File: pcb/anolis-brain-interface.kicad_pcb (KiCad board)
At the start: 2 copper layers, 2 parts, among them U1 RHD2216, U2 Setebos-I

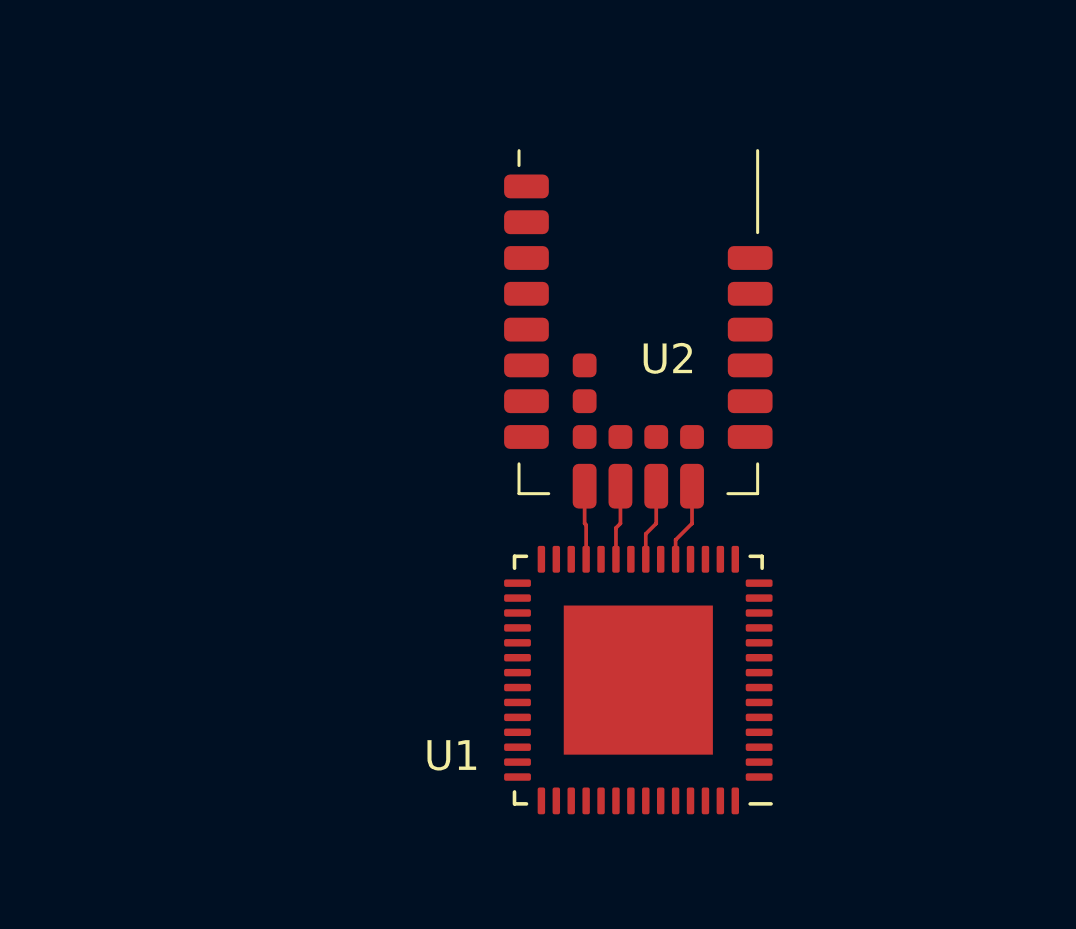
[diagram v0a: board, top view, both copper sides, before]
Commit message: Added uSD socket.
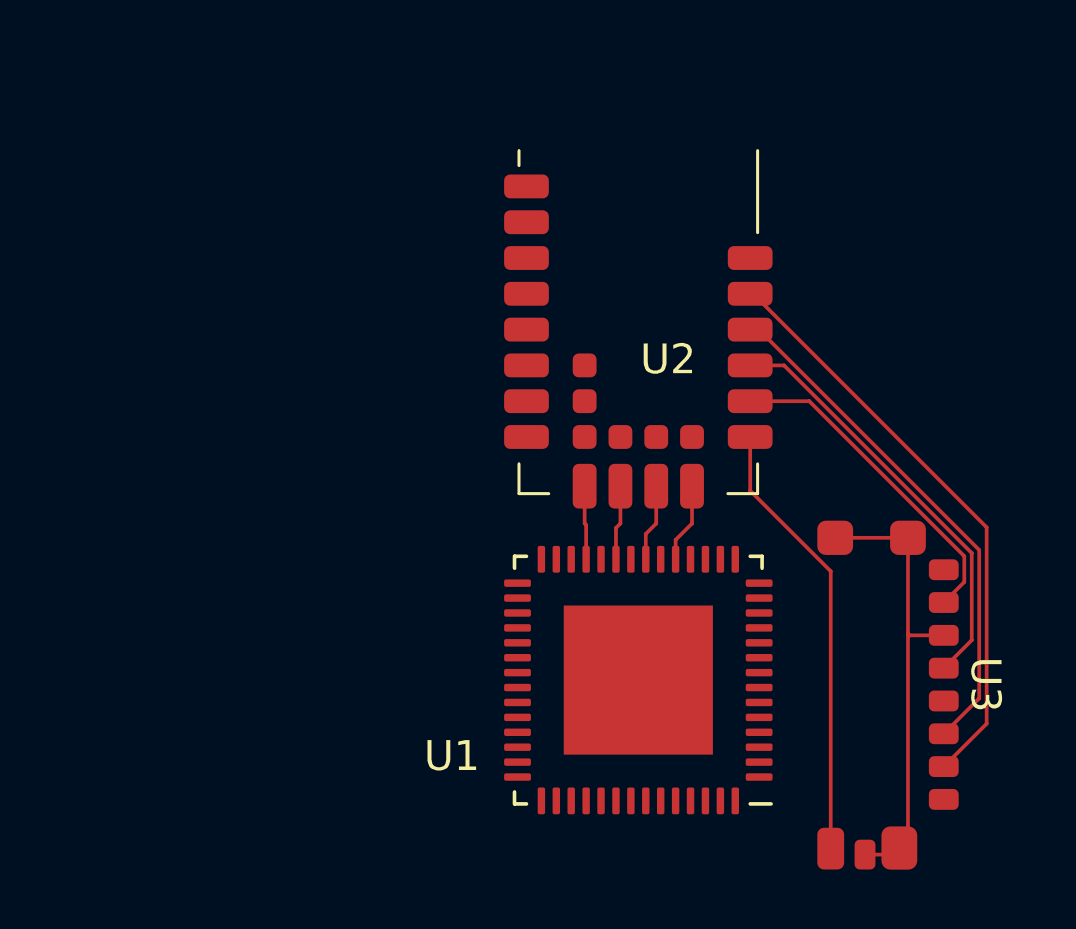
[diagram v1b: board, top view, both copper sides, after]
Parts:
- added U3: 47571-0001, sd:475710001, F.Cu at (155.6, 100.9)
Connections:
- U2 pad 13: unconnected-(U2-P1.08-Pad13) -> /SD_DET
- U2 pad 14: unconnected-(U2-P1.09-Pad14) -> /SD_MISO
- U2 pad 15: unconnected-(U2-P0.11-Pad15) -> /SD_SCLK
- U2 pad 16: unconnected-(U2-P0.12-Pad16) -> /SD_MOSI
- U2 pad 17: unconnected-(U2-P0.03-Pad17) -> /SD_~{CS}
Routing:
- net /SD_~{CS}: track 0.00 -> 19.8 mm
- net /SD_MOSI: track 0.00 -> 17.4 mm
- net /GND: track 0.00 -> 15.4 mm
- net /SD_DET: track 0.00 -> 14.9 mm
- net /SD_SCLK: track 0.00 -> 14.3 mm
- net /SD_MISO: track 0.00 -> 11.2 mm

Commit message: Added power supply.
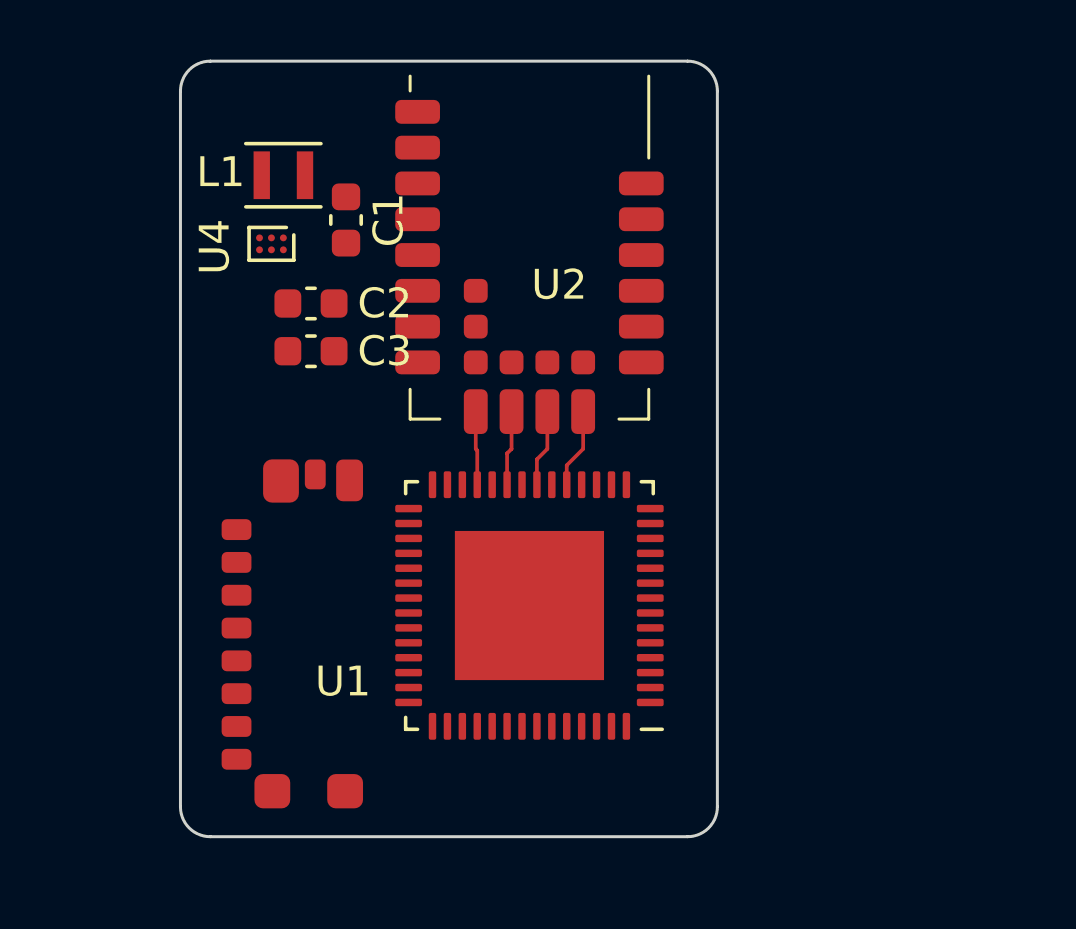
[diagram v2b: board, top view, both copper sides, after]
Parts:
- added C1: 10µF, 16V, Capacitor_SMD:C_0603_1608Metric, F.Cu at (135.6, 85.3)
- added C2: 10µF, 16V, Capacitor_SMD:C_0603_1608Metric, F.Cu at (134.4, 88.1)
- added C3: 10µF, 16V, Capacitor_SMD:C_0603_1608Metric, F.Cu at (134.4, 89.7)
- added L1: VLS201610CX-2R2M-1, 2.2µH, Inductor_SMD:L_Murata_DFE201610P, F.Cu at (133.4, 83.8)
- added U4: TPS610994YFF, Package_BGA:Texas_DSBGA-6_0.855x1.255mm_Layout2x3_P0.4mm_LevelC, F.Cu at (133.1, 86.1)
- moved U3 23.7 mm to (131.9, 99.6), turned to 90 degrees
- moved U1 4.42 mm to (141.7, 98.2)
- moved U2 4.42 mm to (141.7, 86.0)
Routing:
- net /SD_~{CS}: track 19.8 -> 0.00 mm
- net /SD_MOSI: track 17.4 -> 0.00 mm
- net /GND: track 15.4 -> 0.00 mm
- net /SD_DET: track 14.9 -> 0.00 mm
- net /SD_SCLK: track 14.3 -> 0.00 mm
- net /SD_MISO: track 11.2 -> 0.00 mm
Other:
- board outline added: 18 x 26 mm

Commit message: Added capacitors.
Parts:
- added C4: 10µF, 16V, Capacitor_SMD:C_0603_1608Metric, F.Cu at (131.0, 91.8)
- added C5: 10nF, 16V, Capacitor_SMD:C_0402_1005Metric, F.Cu at (136.5, 92.0)
- added C6: 100nF, 16V, Capacitor_SMD:C_0402_1005Metric, F.Cu at (135.3, 92.0)
- added C7: 100nF, 16V, Capacitor_SMD:C_0402_1005Metric, F.Cu at (147.0, 95.5)
- moved U3 0.40 mm to (131.8, 100.0)
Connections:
- U1 pad 28: unconnected-(U1-ADC_REF-Pad28) -> Net-(U1-ADC_REF)

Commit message: Added attachment slits.
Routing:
- net /VDD: track 0.00 -> 1.60 mm
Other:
- board size 18 x 26 mm -> 26 x 26 mm
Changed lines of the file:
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@@
     (property "ki_keywords" "cap capacitor")
     (attr smd)
-    (fp_text reference "C3" (at 2.475 0) (layer "F.SilkS")
+    (fp_text reference "C3" (at -2.575 -0.225) (layer "F.SilkS")
         (effects (font (size 1 1) (thickness 0.15)))
     )
@@
     (property "ki_keywords" "cap capacitor")
     (attr smd)
-    (fp_text reference "C2" (at 2.475 0) (layer "F.SilkS")
+    (fp_text reference "C2" (at -2.575 0) (layer "F.SilkS")
         (effects (font (size 1 1) (thickness 0.15)))
     )
@@
     )
   )
-  (gr_line (start 131 106) (end 147 106)
-    (stroke (width 0.1) (type default)) (layer "Edge.Cuts"))
-  (gr_arc (start 130 81) (mid 130.292893 80.292893) (end 131 80)
-    (stroke (width 0.1) (type default)) (layer "Edge.Cuts"))
-  (gr_line (start 131 80) (end 147 80)
-    (stroke (width 0.1) (type default)) (layer "Edge.Cuts"))
-  (gr_line (start 130 105) (end 130 81)
-    (stroke (width 0.1) (type default)) (layer "Edge.Cuts"))
-  (gr_arc (start 131 106) (mid 130.292893 105.707107) (end 130 105)
-    (stroke (width 0.1) (type default)) (layer "Edge.Cuts"))
-  (gr_arc (start 148 105) (mid 147.707107 105.707107) (end 147 106)
-    (stroke (width 0.1) (type default)) (layer "Edge.Cuts"))
-  (gr_arc (start 147 80) (mid 147.707107 80.292893) (end 148 81)
-    (stroke (width 0.1) (type default)) (layer "Edge.Cuts"))
-  (gr_line (start 148 81) (end 148 105)
-    (stroke (width 0.1) (type default)) (layer "Edge.Cuts"))
+  (gr_arc (start 152 103) (mid 151.12132 105.12132) (end 149 106)
+    (stroke (width 0.1) (type default)) (layer "Edge.Cuts"))
+  (gr_line (start 150 83) (end 150 103)
+    (stroke (width 0.1) (type default)) (layer "Edge.Cuts"))
+  (gr_arc (start 150 103) (mid 149 104) (end 148 103)
+    (stroke (width 0.1) (type default)) (layer "Edge.Cuts"))
+  (gr_line (start 129 106) (end 149 106)
+    (stroke (width 0.1) (type default)) (layer "Edge.Cuts"))
+  (gr_line (start 130 83) (end 130 103)
+    (stroke (width 0.1) (type default)) (layer "Edge.Cuts"))
+  (gr_arc (start 130 103) (mid 129 104) (end 128 103)
+    (stroke (width 0.1) (type default)) (layer "Edge.Cuts"))
+  (gr_arc (start 128 83) (mid 129 82) (end 130 83)
+    (stroke (width 0.1) (type default)) (layer "Edge.Cuts"))
+  (gr_arc (start 126 83) (mid 126.87868 80.87868) (end 129 80)
+    (stroke (width 0.1) (type default)) (layer "Edge.Cuts"))
+  (gr_arc (start 148 83) (mid 149 82) (end 150 83)
+    (stroke (width 0.1) (type default)) (layer "Edge.Cuts"))
+  (gr_line (start 129 80) (end 149 80)
+    (stroke (width 0.1) (type default)) (layer "Edge.Cuts"))
+  (gr_line (start 126 103) (end 126 83)
+    (stroke (width 0.1) (type default)) (layer "Edge.Cuts"))
+  (gr_line (start 128 103) (end 128 83)
+    (stroke (width 0.1) (type default)) (layer "Edge.Cuts"))
+  (gr_arc (start 129 106) (mid 126.87868 105.12132) (end 126 103)
+    (stroke (width 0.1) (type default)) (layer "Edge.Cuts"))
+  (gr_line (start 148 103) (end 148 83)
+    (stroke (width 0.1) (type default)) (layer "Edge.Cuts"))
+  (gr_line (start 152 83) (end 152 103)
+    (stroke (width 0.1) (type default)) (layer "Edge.Cuts"))
+  (gr_arc (start 149 80) (mid 151.12132 80.87868) (end 152 83)
+    (stroke (width 0.1) (type default)) (layer "Edge.Cuts"))
+  (segment (start 133.6 88.125) (end 133.6 89.725) (width 0.125) (layer "F.Cu") (net 53))
   (segment (start 143.5 91.75) (end 143.5 93) (width 0.125) (layer "F.Cu") (net 54))
   (segment (start 143.5 93) (end 142.95 93.55) (width 0.125) (layer "F.Cu") (net 54))
